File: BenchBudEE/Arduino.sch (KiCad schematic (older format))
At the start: 21 parts

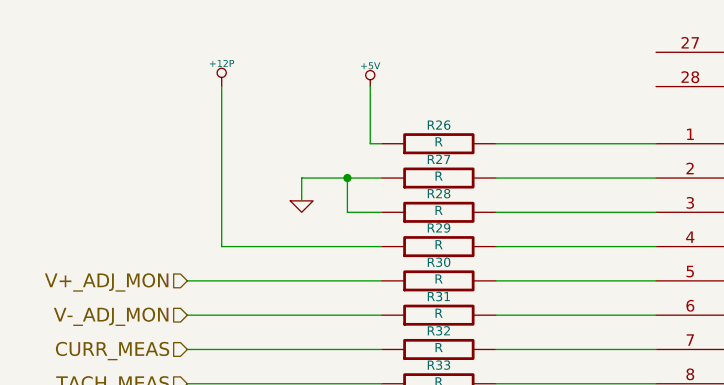
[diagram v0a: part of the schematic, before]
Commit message: Associated and placed the Arduino module.
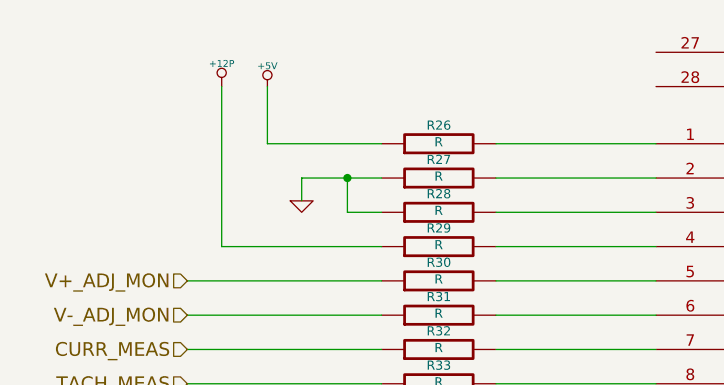
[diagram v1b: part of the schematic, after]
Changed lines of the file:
@@
 	3800 3000 4500 3000
 Wire Wire Line
-	3300 3000 3250 3000
-Wire Wire Line
-	3250 3000 3250 2750
+	2800 3000 3300 3000
 $Comp
 L +5V #PWR61
 U 1 1 53043481
-P 3250 2750
-F 0 "#PWR61" H 3250 2840 20  0001 C CNN
-F 1 "+5V" H 3250 2840 30  0000 C CNN
-F 2 "" H 3250 2750 60  0000 C CNN
-F 3 "" H 3250 2750 60  0000 C CNN
-	1    3250 2750
+P 2800 2750
+F 0 "#PWR61" H 2800 2840 20  0001 C CNN
+F 1 "+5V" H 2800 2840 30  0000 C CNN
+F 2 "" H 2800 2750 60  0000 C CNN
+F 3 "" H 2800 2750 60  0000 C CNN
+	1    2800 2750
 	1    0    0    -1
 $EndComp
@@
 Wire Wire Line
 	7950 4300 8650 4300
+Wire Wire Line
+	2800 3000 2800 2750
 $EndSCHEMATC

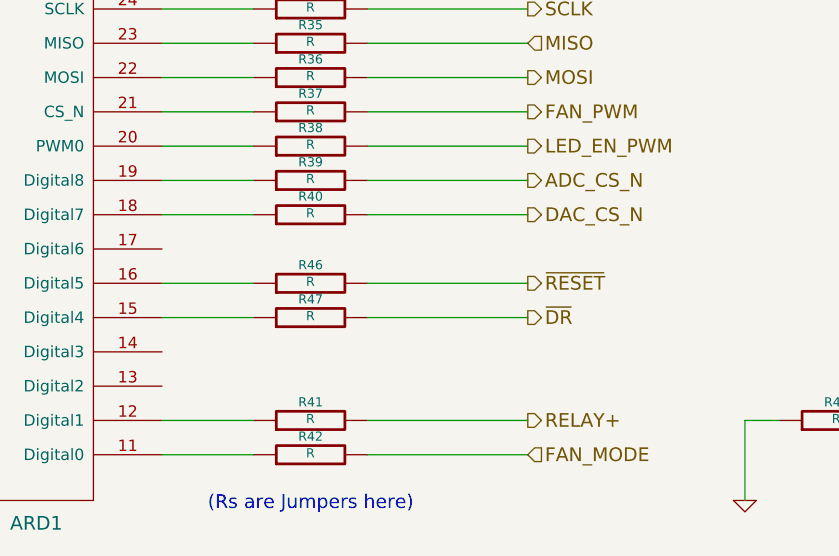
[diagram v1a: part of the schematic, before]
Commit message: Associating the current/fan driver module components.
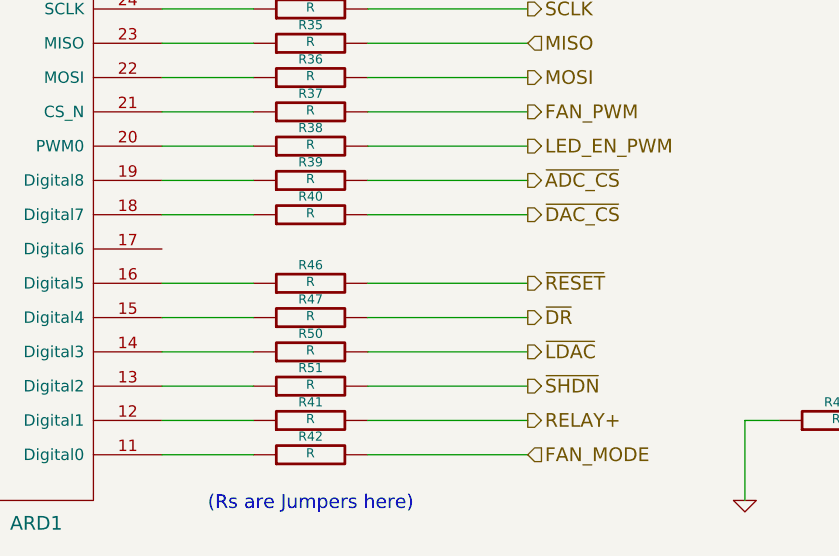
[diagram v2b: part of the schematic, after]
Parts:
- added R50, R51: R, ~, symbol R
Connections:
- net at ARD1.13 (Digital2): now also R51.1
- net at ARD1.14 (Digital3): now also R50.1
- net ADC_CS_N renamed ~ADC_CS
- net DAC_CS_N renamed ~DAC_CS
- new net ~LDAC: R50.2
- new net ~SHDN: R51.2
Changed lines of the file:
@@
 SCLK
 Text HLabel 8650 3850 2    60   Output ~ 0
-DAC_CS_N
+~DAC_CS
 Text HLabel 8650 3400 2    60   Output ~ 0
 FAN_PWM
@@
 	7050 4750 7450 4750
 $Comp
-L GND #PWR62
+L GND #PWR65
 U 1 1 52F915E6
 P 9600 5100
-F 0 "#PWR62" H 9600 5100 30  0001 C CNN
+F 0 "#PWR65" H 9600 5100 30  0001 C CNN
 F 1 "GND" H 9600 5030 30  0001 C CNN
 F 2 "" H 9600 5100 60  0000 C CNN
@@
 	7950 3550 8650 3550
 Text HLabel 8650 3700 2    60   Output ~ 0
-ADC_CS_N
+~ADC_CS
 $Comp
 L R R39
@@
 	2600 3450 2600 2750
 $Comp
-L +12P #PWR59
+L +12P #PWR62
 U 1 1 52FAFE2B
 P 2600 2750
-F 0 "#PWR59" H 2600 2720 30  0001 C CNN
+F 0 "#PWR62" H 2600 2720 30  0001 C CNN
 F 1 "+12P" H 2600 2850 30  0000 C CNN
 F 2 "" H 2600 2750 60  0000 C CNN
@@
 	2800 3000 3300 3000
 $Comp
-L +5V #PWR61
+L +5V #PWR63
 U 1 1 53043481
 P 2800 2750
-F 0 "#PWR61" H 2800 2840 20  0001 C CNN
+F 0 "#PWR63" H 2800 2840 20  0001 C CNN
 F 1 "+5V" H 2800 2840 30  0000 C CNN
 F 2 "" H 2800 2750 60  0000 C CNN
@@
 	2950 3150 2950 3250
 $Comp
-L GND #PWR60
+L GND #PWR64
 U 1 1 5304350C
 P 2950 3250
-F 0 "#PWR60" H 2950 3250 30  0001 C CNN
+F 0 "#PWR64" H 2950 3250 30  0001 C CNN
 F 1 "GND" H 2950 3180 30  0001 C CNN
 F 2 "" H 2950 3250 60  0000 C CNN
@@
 Wire Wire Line
 	2800 3000 2800 2750
+$Comp
+L R R51
+U 1 1 5308A480
+P 7700 4600
+F 0 "R51" V 7780 4600 40  0000 C CNN
+F 1 "R" V 7707 4601 40  0000 C CNN
+F 2 "~" V 7630 4600 30  0000 C CNN
+F 3 "~" H 7700 4600 30  0000 C CNN
+	1    7700 4600
+	0    -1   -1   0
+$EndComp
+$Comp
+L R R50
+U 1 1 5308A486
+P 7700 4450
+F 0 "R50" V 7780 4450 40  0000 C CNN
+F 1 "R" V 7707 4451 40  0000 C CNN
+F 2 "~" V 7630 4450 30  0000 C CNN
+F 3 "~" H 7700 4450 30  0000 C CNN
+	1    7700 4450
+	0    -1   -1   0
+$EndComp
+Wire Wire Line
+	7450 4450 7050 4450
+Wire Wire Line
+	7050 4600 7450 4600
+Text HLabel 8650 4450 2    60   Output ~ 0
+~LDAC
+Text HLabel 8650 4600 2    60   Output ~ 0
+~SHDN
+Wire Wire Line
+	7950 4600 8650 4600
+Wire Wire Line
+	7950 4450 8650 4450
 $EndSCHEMATC
